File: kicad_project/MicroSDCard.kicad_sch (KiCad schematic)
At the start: 10 parts, among them J8 DM3AT, U14 ADG733BRU, U21 TXS0104EPW

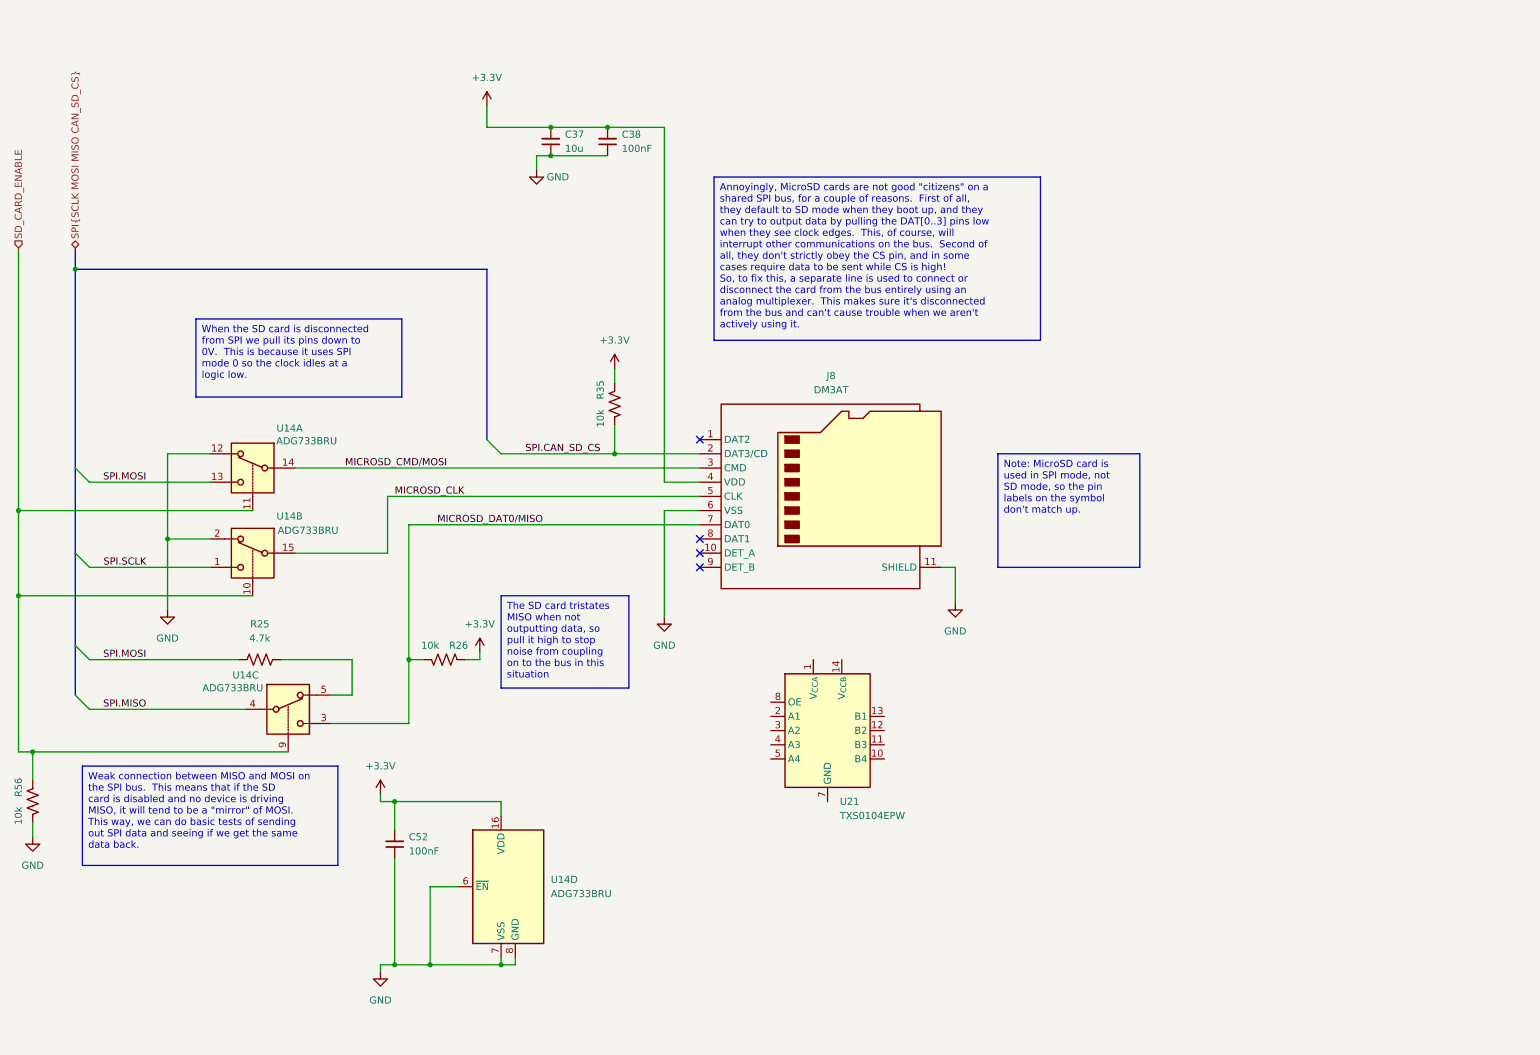
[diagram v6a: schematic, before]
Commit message: Finish new SD card schematic, ERC passing!
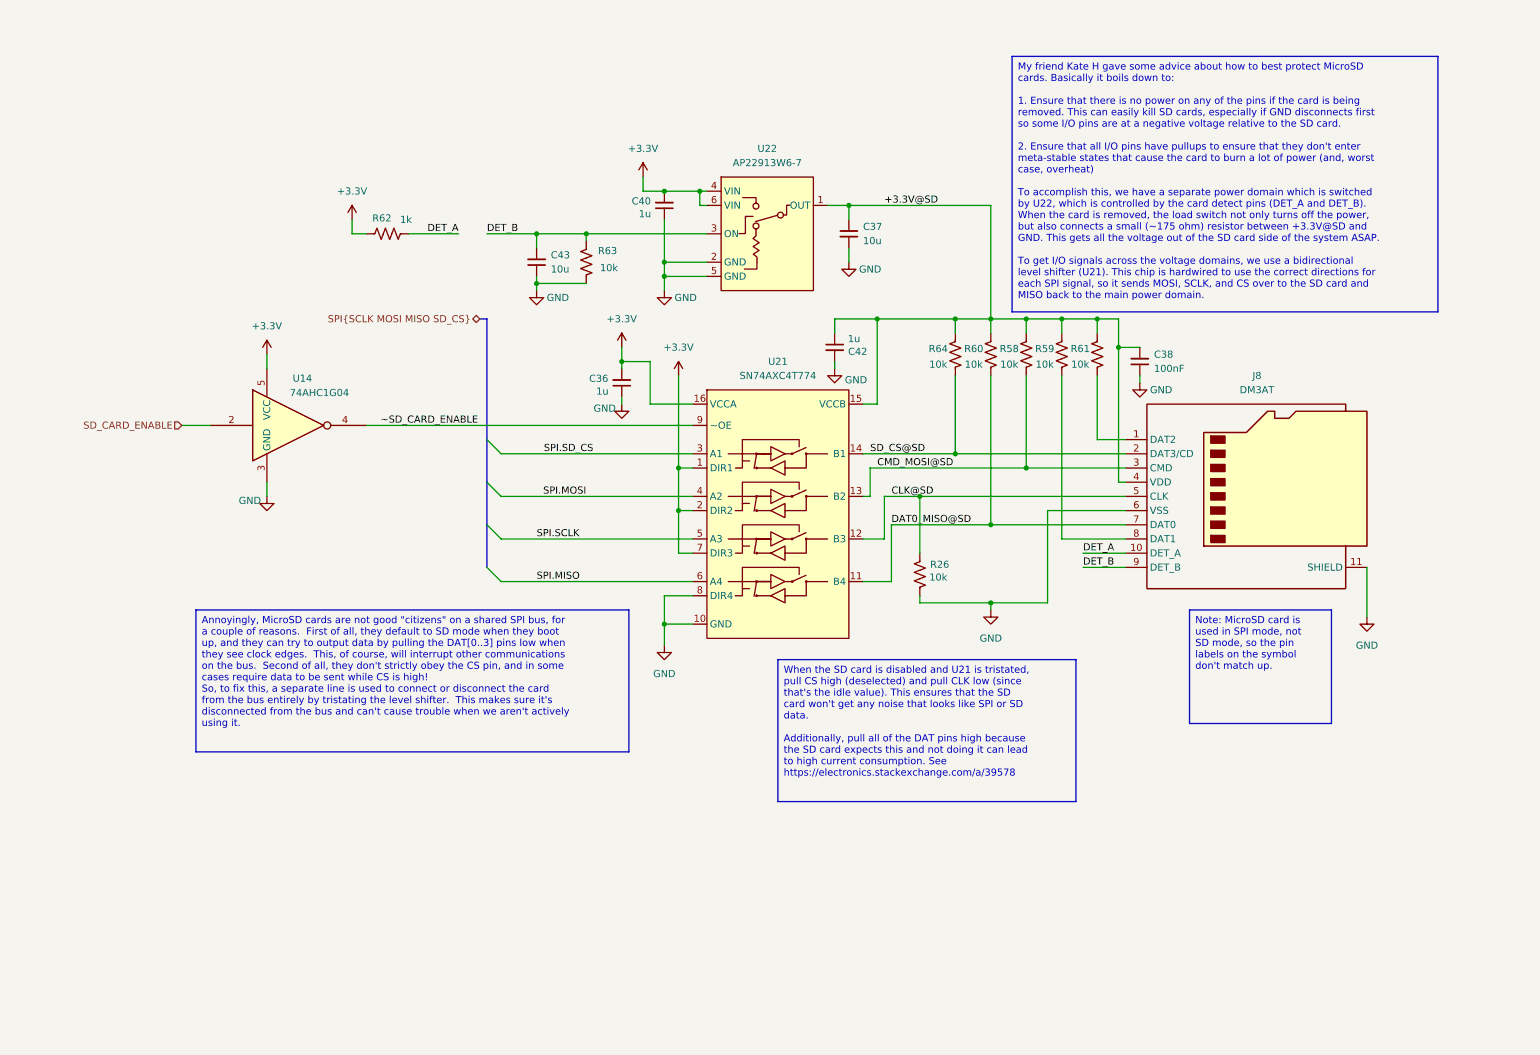
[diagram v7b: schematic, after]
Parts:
- removed C52: 100nF, Capacitor_SMD:C_1206_3216Metric, symbol Device:C_Small
- removed R25: 4.7k, Resistor_SMD:R_1206_3216Metric, symbol Device:R_US
- removed R35, R56: 10k, Resistor_SMD:R_1206_3216Metric, symbol Device:R_US
- removed U14: ADG733BRU, Package_SO:TSSOP-16_4.4x5mm_P0.65mm, symbol Analog_Switch:ADG733BRU
- removed U21: TXS0104EPW, Package_SO:TSSOP-14_4.4x5mm_P0.65mm, symbol Logic_LevelTranslator:TXS0104EPW
- added C36, C40, C42: 1u, Capacitor_SMD:C_1206_3216Metric, symbol Device:C_Small
- added C43: 10u, Capacitor_SMD:C_1206_3216Metric, symbol Device:C_Small
- added R58, R59, R60, R61, R63, R64: 10k, Resistor_SMD:R_1206_3216Metric, symbol Device:R_US
- added R62: 1k, Resistor_SMD:R_1206_3216Metric, symbol Device:R_US
- added U14: 74AHC1G04, Package_TO_SOT_SMD:SOT-23-5, symbol 74xGxx:74AHC1G04
- added U21: SN74AXC4T774, Package_SO:TSSOP-16_4.4x5mm_P0.65mm, symbol project libraries:SN74AXC4T774
- added U22: AP22913W6-7, Package_TO_SOT_SMD:SOT-23-6, symbol project libraries:AP22913W6-7
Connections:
- net +3.3V: now also C36.2, C40.2, R62.1, U14.5 (VCC), U21.1 (DIR1), U21.16 (VCCA), U21.2 (DIR2), U21.7 (DIR3), U22.4 (VIN), U22.6 (VIN); no longer C37.2, C38.2, J8.4 (VDD), R26.2
- net GND: now also R26.2, C36.1, C40.1, C42.2, C43.1, R63.2, U14.3 (GND), U21.10 (GND), U21.8 (DIR4), U22.2 (GND), U22.5 (GND)
- net SD_CARD_ENABLE: now also U14.2
- net SPI.MISO: now also U21.6 (A4)
- net SPI.MOSI: now also U21.4 (A2)
- net SPI.SCLK: now also U21.5 (A3)
- net at J8.1 (DAT2): now also R61.2
- net DET_A: now reaches J8.10 (DET_A)
- net DET_A: now also R62.2
- net at J8.8 (DAT1): now also R59.2
- net DET_B: now reaches J8.9 (DET_B)
- net DET_B: now also C43.2, R63.1, U22.3 (ON)
- net MICROSD_CLK renamed CLK@SD
- net CLK@SD: now also R26.1, U21.12 (B3)
- net MICROSD_CMD/MOSI renamed CMD_MOSI@SD
- net CMD_MOSI@SD: now also R58.2, U21.13 (B2)
- net MICROSD_DAT0/MISO renamed DAT0_MISO@SD
- net DAT0_MISO@SD: now also R60.2, U21.11 (B4); no longer R26.1
- net SPI.CAN_SD_CS renamed SD_CS@SD
- net SD_CS@SD: now also R64.2, U21.14 (B1)
- new net +3.3V@SD: C37.2, C38.2, C42.1, J8.4 (VDD), R58.1, R59.1, R60.1, R61.1, R64.1, U21.15 (VCCB), U22.1 (OUT)
- new net SPI.SD_CS: U21.3 (A1)
- new net ~SD_CARD_ENABLE: U14.4, U21.9 (~OE)
- no-connect marks 4 -> 0
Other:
- moved on the sheet: J8

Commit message: Fix some BOM isues
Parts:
- U21: SKU (none) -> 296-SN74AXC4T774PWRCT-ND
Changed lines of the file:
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@@
+			)
+		)
+		(property "SKU" "296-SN74AXC4T774PWRCT-ND"
+			(at 165.1 93.98 0)
+			(effects
+				(font
+					(size 1.27 1.27)
+				)
+				(hide yes)
 			)
 		)
